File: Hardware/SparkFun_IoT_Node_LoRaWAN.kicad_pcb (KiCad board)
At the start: 4 copper layers, 50.8 x 76.2 mm, 71 parts, among them J1 USB_C_Receptacle, J2 JST_2mm_LiPo, J3 Qwiic_RA, SW1 SMD_4.6x2.8mm_h2.5mm, SW2 SMD_4.6x2.8mm_h2.5mm, U4 W25Q128JVPIM, U5 RT9080-3.3, U6 MCP73831, U7 MAX17048, U8 LM66200, U9 RT9080-3.3

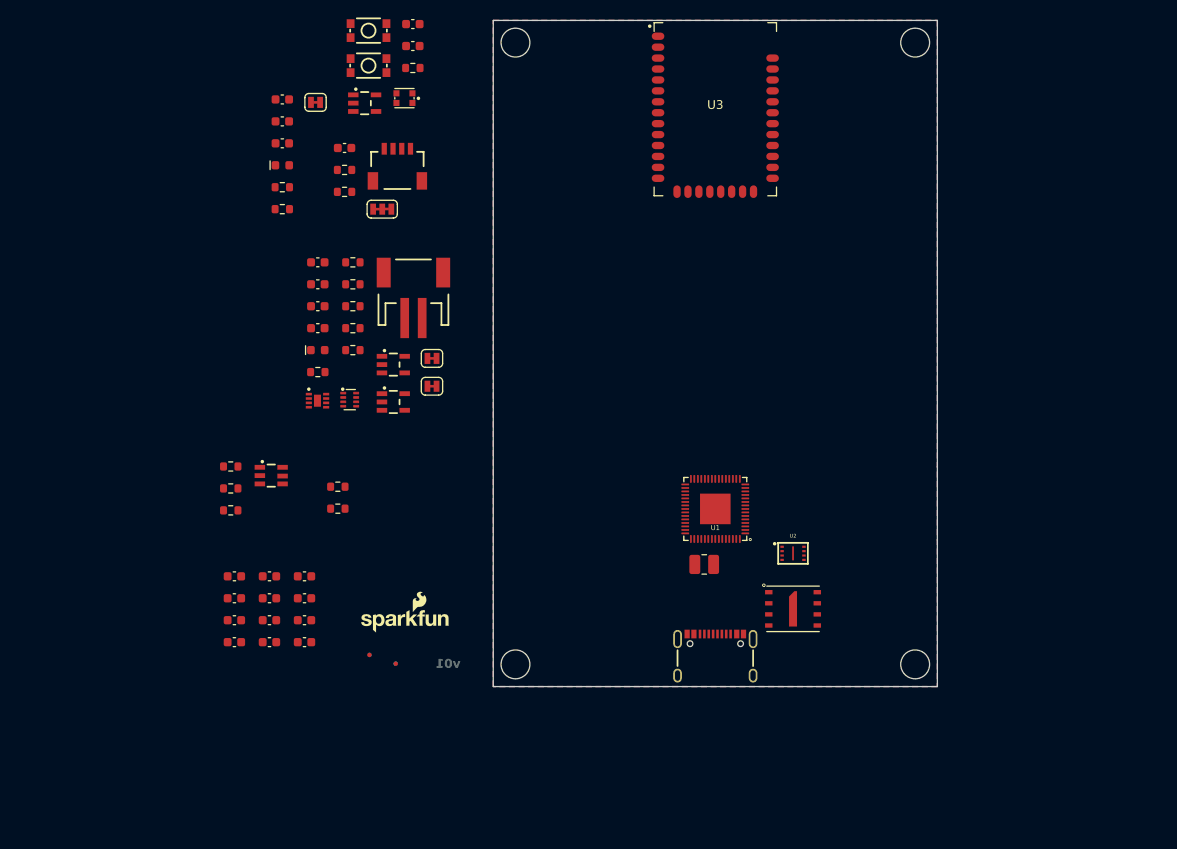
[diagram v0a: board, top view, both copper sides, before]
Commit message: v01 schematic updates
Add remaining schematic components
Split schematic into multiple sheets
Still need to define pinouts for RP2350, XBLR, and headers
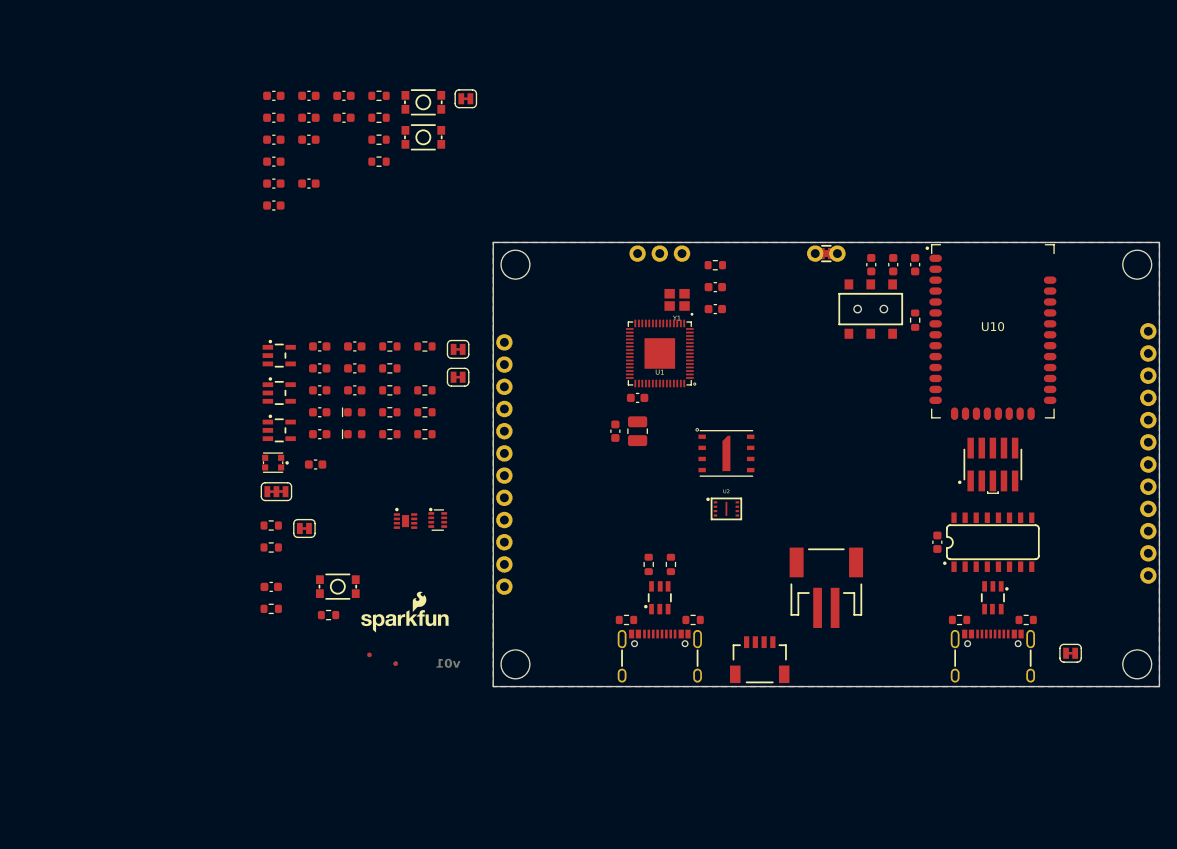
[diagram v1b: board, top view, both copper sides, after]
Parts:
- added C23: 10uF, SparkFun-Capacitor:C_0603_1608Metric, F.Cu at (158.8, 76.2)
- added C24: 1.0uF, SparkFun-Capacitor:C_0603_1608Metric, F.Cu at (161.3, 76.2)
- added C25: 10pF, SparkFun-Capacitor:C_0603_1608Metric, F.Cu at (163.8, 76.2)
- added C26: 10uF, SparkFun-Capacitor:C_0603_1608Metric, F.Cu at (95.2, 99.1)
- added C27: 0.1uF, SparkFun-Capacitor:C_0603_1608Metric, F.Cu at (166.4, 108.0)
- added C28: 2.2uF, SparkFun-Capacitor:C_0603_1608Metric, F.Cu at (90.2, 113.1)
- added C29: 15pF, SparkFun-Capacitor:C_0603_1608Metric, F.Cu at (141.0, 81.3)
- added C30: 15pF, SparkFun-Capacitor:C_0603_1608Metric, F.Cu at (141.0, 78.8)
- added D5: DT1042-04SO, SparkFun-Semiconductor-Standard:SOT23-6, F.Cu at (172.7, 114.3)
- added J4: USB_C_Receptacle, SparkFun-Connector:USB-C_16, F.Cu at (172.7, 118.1)
- added J5: USB_C_Receptacle, SparkFun-Connector:USB-C_16, F.Cu at (134.6, 118.1)
- added J6: SWD, SparkFun-Connector:2x5_1.27mm_SMD_Unshrouded, F.Cu at (172.7, 99.1)
- added J7: Conn_01x12, SparkFun-Connector:1x12, F.Cu at (116.8, 85.1)
- added J8: Conn_01x12, SparkFun-Connector:1x12, F.Cu at (190.5, 83.8)
- added JP5: ~, SparkFun-Jumper:Jumper_2_NC_Trace, F.Cu at (181.6, 120.7)
- added JP6: Measure, SparkFun-Jumper:Jumper_2_PTH_SMD_Combo-NC, F.Cu at (153.7, 74.9)
- added JP7: ~, SparkFun-Jumper:Jumper_2_NC_Trace, F.Cu at (94.0, 106.4)
- added R17: 5.1k, SparkFun-Resistor:R_0603_1608Metric, F.Cu at (176.5, 116.8)
- added R18: 5.1k, SparkFun-Resistor:R_0603_1608Metric, F.Cu at (168.9, 116.8)
- added R19: 100k, SparkFun-Resistor:R_0603_1608Metric, F.Cu at (107.8, 93.1)
- added R20: 2.2k, SparkFun-Resistor:R_0603_1608Metric, F.Cu at (107.8, 95.6)
- added R21: 10k, SparkFun-Resistor:R_0603_1608Metric, F.Cu at (96.7, 116.3)
- added R22: 10k, SparkFun-Resistor:R_0603_1608Metric, F.Cu at (163.8, 82.5)
- added R23: 10, SparkFun-Resistor:R_0603_1608Metric, F.Cu at (90.2, 115.6)
- added R24: 1k, SparkFun-Resistor:R_0603_1608Metric, F.Cu at (90.2, 108.5)
- added R25: 1k, SparkFun-Resistor:R_0603_1608Metric, F.Cu at (141.0, 76.3)
- added SW3: DPDT_Slide_SMD_7.2x3.5mm, SparkFun-Switch:Slide_DPDT_SMD_7.2x3.5mm, F.Cu at (158.8, 81.3)
- added SW4: SMD_4.6x2.8mm_h2.5mm, SparkFun-Switch:Push_SMD_4.6x2.8mm, F.Cu at (97.8, 113.0)
- added U10: ~, SparkFun_IoT_Node_LoRaWAN:XBee_LR, F.Cu at (172.7, 83.8)
- added Y1: ~, SparkFun-Clocks:CRYSTAL-SMD-2X2.5MM, F.Cu at (136.6, 80.2)
- C2, C6: value 2.2uF -> 0.1uF
- C20: value 0.1uF -> 10uF
- C22: value 10uF -> 0.1uF
- C5, C8: value 0.1uF -> 2.2uF
- D1: value Yellow -> WS2812B; footprint SparkFun-LED:LED_0603_1608Metric -> SparkFun-LED:WS2812-2020
- D2: value WS2812B -> Yellow; footprint SparkFun-LED:WS2812-2020 -> SparkFun-LED:LED_0603_1608Metric
- J1: value USB_C_Receptacle -> Conn_01x03; footprint SparkFun-Connector:USB-C_16 -> SparkFun-Connector:1x03
- JP3: footprint SparkFun-Jumper:Jumper_3_NC-2_Trace -> SparkFun-Jumper:Jumper_2_NC_Trace
- JP4: footprint SparkFun-Jumper:Jumper_2_NC_Trace -> SparkFun-Jumper:Jumper_3_NC-2_Trace
- R10, R9: value 2.2k -> 4.7k
- R11: value 100k -> 2.2k
- R13: value 4.7k -> 2.2k
- R5, R6: value 100k -> 10k
- R8: value 4.7k -> 100k
- U3: value ~ -> CH340C; footprint SparkFun_IoT_Node_LoRaWAN:XBee_LR -> SparkFun-Semiconductor-Standard:SO-16
- U5: value RT9080-3.3 -> LM66200; footprint SparkFun-Semiconductor-Standard:SOT23-5 -> SparkFun-Semiconductor-Standard:SOT-583-8
- U6: value MCP73831 -> RT9080-3.3
- U7: value MAX17048 -> MCP73831; footprint SparkFun-Semiconductor-Standard:DFN-8 -> SparkFun-Semiconductor-Standard:SOT23-5
- U8: value LM66200 -> MAX17048; footprint SparkFun-Semiconductor-Standard:SOT-583-8 -> SparkFun-Semiconductor-Standard:DFN-8
- moved J3 70.0 mm to (146.1, 119.4)
- moved C21 60.2 mm to (98.5, 56.9)
- moved C22 60.2 mm to (98.5, 59.4)
- moved U3 58.8 mm to (172.7, 108.0), turned to 90 degrees
- moved J2 57.7 mm to (153.7, 111.8)
- moved C17 55.1 mm to (94.5, 61.9)
- moved C15 55.1 mm to (94.5, 56.9)
- moved C16 55.1 mm to (94.5, 59.4)
- moved R11 54.8 mm to (90.2, 106.0)
- moved C13 50.1 mm to (90.5, 66.9)
- moved C11 50.1 mm to (90.5, 61.9)
- moved C12 50.1 mm to (90.5, 64.4)
- moved C14 50.1 mm to (90.5, 69.4)
- moved R4 48.4 mm to (133.3, 110.5), turned to -90 degrees
- moved D4 46.6 mm to (134.6, 114.3), turned to 90 degrees
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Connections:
- C12 pad 1: 3.3V -> 1.1V
- C14 pad 1: 3.3V -> 1.1V
- C16 pad 1: 3.3V -> 1.1V
- C18 pad 1: 3.3V -> 1.1V
- C19 pad 1: 1.8V -> 3.3V
- C2 pad 1: 3.3V -> 3.3V_P
- C20 pad 1: 1.8V -> 3.3V
- C21 pad 1: 1.8V -> 3.3V
- C22 pad 1: 1.8V -> 3.3V
- C3 pad 1: VBUS -> 3.3V
- C4 pad 1: VBATT -> VBUS
- C6 pad 1: VIN -> VBATT
- C7 pad 1: 3.3V_P -> VIN
- D1 pad 1: Net-(D1-K) -> LED_OUT
- D1 pad 2: Net-(D1-A) -> GND
- D2 pad 1: LED_OUT -> Net-(D2-K)
- D2 pad 2: GND -> Net-(D2-A)
- JP1 pad 1: Net-(J1-SHIELD) -> Net-(J5-SHIELD)
- JP2 pad 2: Net-(D1-A) -> Net-(D2-A)
- JP3 pad 2: 3.3V_P -> 3.3V
- JP4 pad 2: 3.3V -> 3.3V_P
- L1 pad 1: 1.8V -> 1.1V
- R1 pad 1: Net-(J1-CC2) -> Net-(J5-CC2)
- R10 pad 2: SCL -> Net-(D3-A)
- R11 pad 1: PERIPHERAL_POWER -> Net-(U7-PROG)
- R11 pad 2: 3.3V -> GND
- R12 pad 2: ~{BOOT} -> PSRAM_~{CS}
- R13 pad 1: Net-(JP4-A) -> Net-(JP4-B)
- R13 pad 2: Net-(D3-A) -> SDA
- R14 pad 2: QSPI_~{CS} -> ~{RESET}
- R16 pad 2: PSRAM_~{CS} -> QSPI_~{CS}
- R2 pad 1: Net-(J1-CC1) -> Net-(J5-CC1)
- R5 pad 1: Net-(U5-EN) -> 3.3V
- R5 pad 2: VIN -> REGION
- R6 pad 1: 3.3V -> REGION
- R6 pad 2: BAT_POWER -> GND
- R7 pad 1: Net-(U6-PROG) -> 3.3V
- R7 pad 2: GND -> BAT_POWER
- R8 pad 1: VBUS -> ~{ON}
- R8 pad 2: Net-(JP2-A) -> GND
- R9 pad 1: Net-(JP3-B) -> VBUS
- R9 pad 2: SDA -> Net-(JP2-A)
- SW1 pad 2: ~{RESET} -> ~{BOOT}
- SW2 pad 2: ~{BOOT} -> ~{RESET}
- U1 pad 21: unconnected-(U1-XIN-Pad21) -> Net-(U1-XIN)
- U1 pad 22: unconnected-(U1-XOUT-Pad22) -> Net-(U1-XOUT)
- U1 pad 23: 1.8V -> 1.1V
- U1 pad 24: unconnected-(U1-SWCLK-Pad24) -> RP2350_SWCLK
- U1 pad 25: unconnected-(U1-SWDIO-Pad25) -> RP2350_SWDIO
- U1 pad 39: 1.8V -> 1.1V
- U1 pad 50: 1.8V -> 1.1V
- U1 pad 6: 1.8V -> 1.1V
- U3 pad 10: GND -> unconnected-(U3-~{DSR}-Pad10)
- U3 pad 12: GND -> unconnected-(U3-~{DCD}-Pad12)
- U3 pad 16: unconnected-(U3-SPI_MISO/DIO15-Pad16) -> 3.3V
- U3 pad 2: 3.3V -> XBLR_USB_TX
- U3 pad 3: XBLR_TX -> XBLR_USB_RX
- U3 pad 4: XBLR_RX -> 3.3V
- U3 pad 5: unconnected-(U3-DIO12-Pad5) -> XBLR_USB_DP
- U3 pad 6: unconnected-(U3-~{RESET}-Pad6) -> XBLR_USB_DN
- U5 pad 1: VIN -> GND
- U5 pad 2: GND -> VIN
- U5 pad 3: Net-(U5-EN) -> VBATT
- U5 pad 4: unconnected-(U5-NC-Pad4) -> ~{ON}
- U5 pad 5: 3.3V -> GND
- U6 pad 1: Net-(D1-K) -> VIN
- U6 pad 3: VBATT -> VIN
- U6 pad 4: VBUS -> unconnected-(U6-NC-Pad4)
- U6 pad 5: Net-(U6-PROG) -> 3.3V
- U7 pad 1: GND -> Net-(D2-K)
- U7 pad 2: VBATT -> GND
- U7 pad 3: unconnected-(U7-VDD-Pad3) -> VBATT
- U7 pad 4: GND -> VBUS
- U7 pad 5: FUEL_GAUGE_~{ALRT} -> Net-(U7-PROG)
- U8 pad 2: VIN -> VBATT
- U8 pad 3: VBATT -> unconnected-(U8-VDD-Pad3)
- U8 pad 5: GND -> FUEL_GAUGE_~{ALRT}
- U8 pad 6: VBUS -> GND
- U8 pad 7: VIN -> SCL
- U8 pad 8: BAT_POWER -> SDA
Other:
- board size 50.8 x 76.2 mm -> 76.2 x 50.8 mm

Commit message: Initial board layout
Board outline determined based off selected enclosure
Clusters of components placed and routed
Waiting for feedback before finishing routing
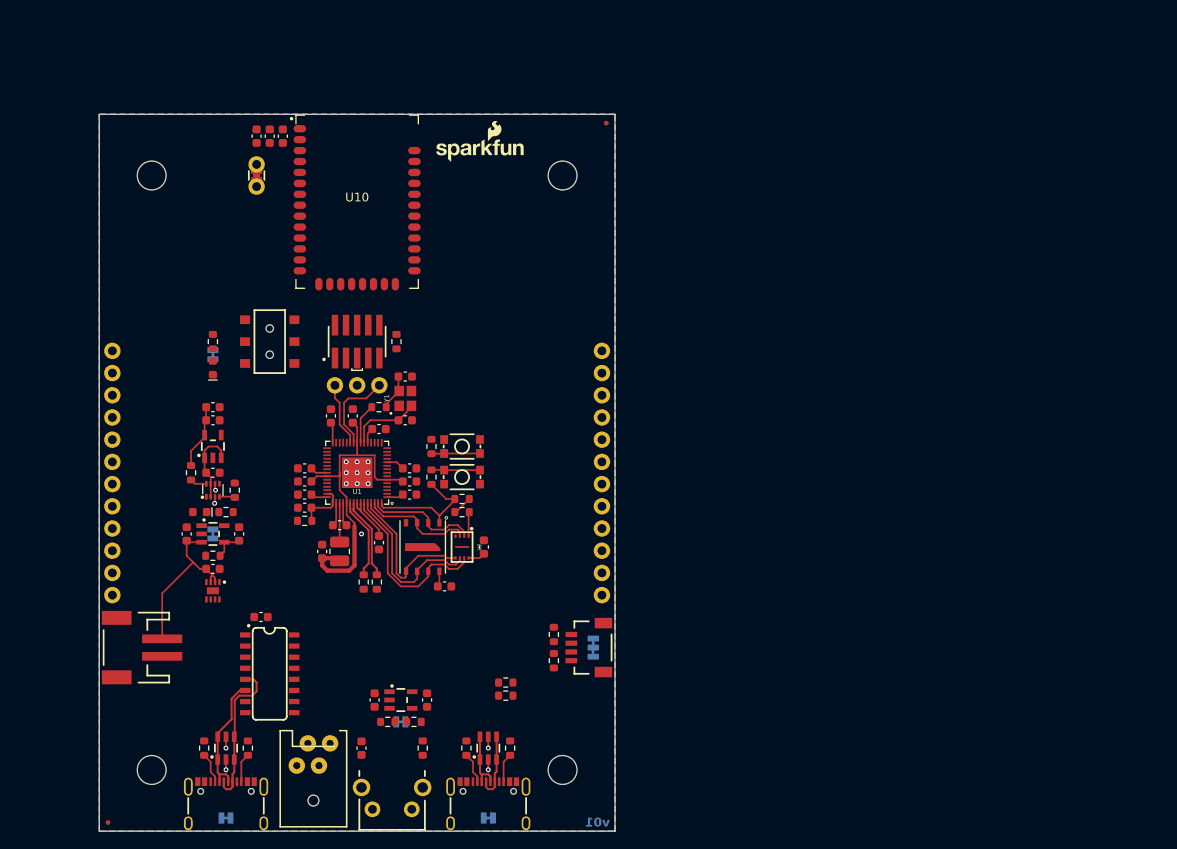
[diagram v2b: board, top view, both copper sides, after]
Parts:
- D1: value WS2812B -> WS2812B_CBI; footprint SparkFun-LED:WS2812-2020 -> SparkFun-LED:WS2812B-CBI
- JP1, JP2, JP3, JP4, JP5, JP7: moved to B.Cu
- ST1, ST2, ST3, ST4: value Stand_off -> Standoff
- SW4: value SMD_4.6x2.8mm_h2.5mm -> PTH_RA_h7.5mm; footprint SparkFun-Switch:Push_SMD_4.6x2.8mm -> SparkFun-Switch:Push_PTH_RA_8-020_h7.5mm
- moved J8 122.3 mm to (72.0, 114.0), turned to 90 degrees
- moved ST4 113.4 mm to (76.5, 134.0)
- moved JP5 98.4 mm to (85.0, 139.5), turned to 180 degrees
- moved R17 90.2 mm to (87.5, 131.5), turned to 90 degrees
- moved D5 89.4 mm to (85.0, 131.5), turned to 90 degrees
- moved J4 89.3 mm to (85.0, 135.0)
- moved R18 87.6 mm to (82.5, 131.5), turned to 90 degrees
- moved ST3 87.5 mm to (123.5, 134.0)
- moved U3 84.1 mm to (90.0, 123.0), turned to 0 degrees
- moved JP1 82.3 mm to (115.0, 139.5), turned to 180 degrees
- moved J2 80.1 mm to (74.0, 120.0), turned to 90 degrees
- moved C27 77.8 mm to (89.0, 116.5), turned to 180 degrees
- moved U10 74.2 mm to (100.0, 69.0)
- moved J6 74.1 mm to (100.0, 85.0)
- moved C25 73.8 mm to (91.5, 61.5)
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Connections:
- net Net-(D4-I/O1) renamed /RP2350/USB_D-
- net Net-(D4-I/O2) renamed /RP2350/USB_D+
- net USB_DN renamed RP2350_USB_D-
- net USB_DP renamed RP2350_USB_D+
- net XBLR_USB_DN renamed XBLR_USB_D-
- net XBLR_USB_DP renamed XBLR_USB_D+
- D1 pad 1: LED_OUT -> LED_IN
- D1 pad 2: GND -> 3.3V_P
- D1 pad 3: LED_IN -> GND
- D1 pad 4: 3.3V_P -> LED_OUT
- U8 pad 3: unconnected-(U8-VDD-Pad3) -> VBATT
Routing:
- net 1.1V: track 0.00 -> 38.2 mm
- net 3.3V: track 0.00 -> 33.9 mm
- net QSPI_D3: track 0.00 -> 21.2 mm
- net VBATT: track 0.00 -> 20.1 mm, vias 0 -> 1
- net QSPI_SCLK: track 0.00 -> 19.7 mm
- net QSPI_D0: track 0.00 -> 17.9 mm
- net XBLR_USB_D+: track 0.00 -> 17.2 mm
- net QSPI_~{CS}: track 0.00 -> 14.3 mm
- net XBLR_USB_D-: track 0.00 -> 13.9 mm
- net QSPI_D1: track 0.00 -> 13.0 mm
- net QSPI_D2: track 0.00 -> 13.0 mm
- net RP2350_SWCLK: track 0.00 -> 9.89 mm
- net RP2350_USB_D-: track 0.00 -> 9.35 mm
- net RP2350_USB_D+: track 0.00 -> 9.35 mm
- net VIN: track 0.00 -> 8.70 mm
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- added copper zone on In2.Cu, net 3.3V
- added copper zone on B.Cu, net GND
- added copper zone on F.Cu, net GND
- added copper zone on In1.Cu, net GND
- removed copper zone on B.Cu, net (none)
- removed copper zone on F.Cu, net (none)
- removed copper zone on In1.Cu, net (none)
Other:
- board size 76.2 x 50.8 mm -> 59 x 82 mm

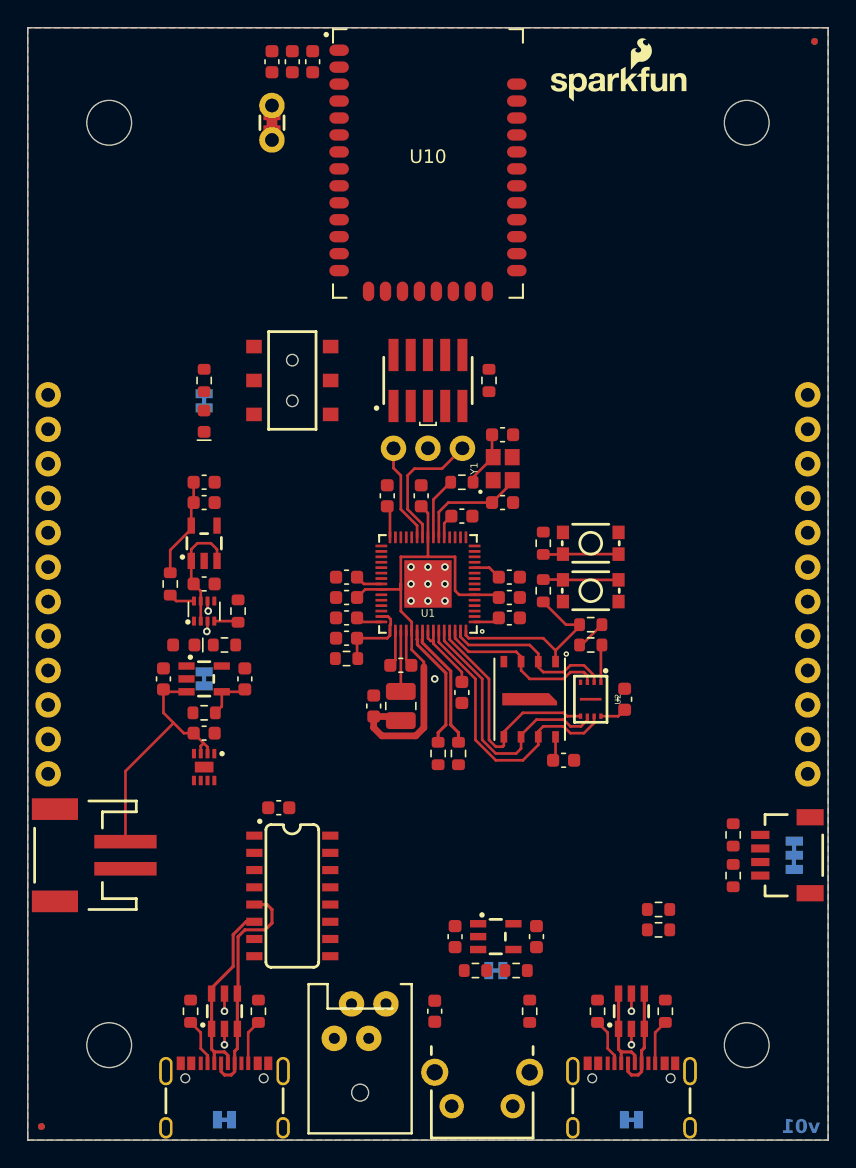
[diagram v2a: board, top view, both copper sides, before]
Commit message: Review updates
Remove region selection resistors
Add uSD card connector
Move XBLR USB connector within enclosure
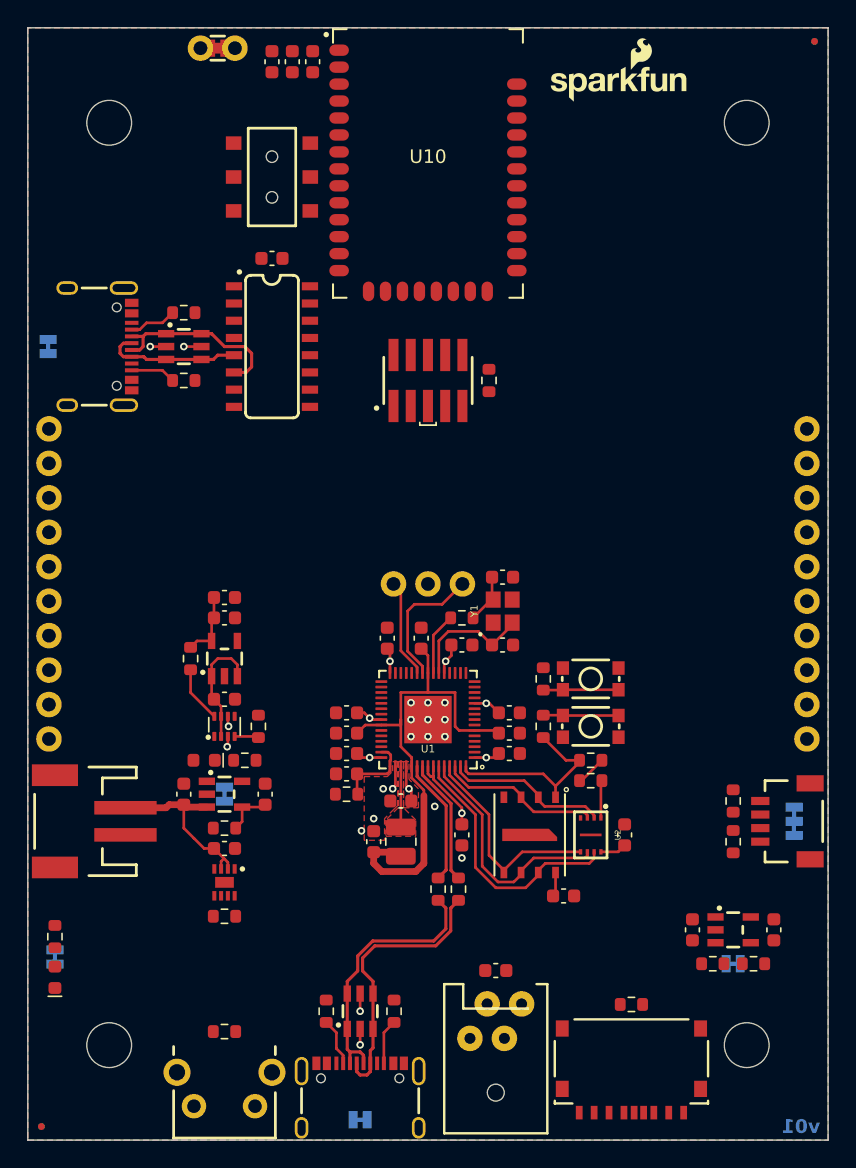
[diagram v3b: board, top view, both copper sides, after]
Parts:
- added J9: microSD_Friction, SparkFun-Connector:microSD_Friction_Fit_Atom, F.Cu at (115.0, 135.0)
- J7, J8: footprint SparkFun-Connector:1x12 -> SparkFun-Connector:1x10
- moved JP5 58.5 mm to (72.0, 82.5), turned to 90 degrees
- moved J7 56.0 mm to (72.1, 111.4)
- moved J8 56.0 mm to (127.9, 111.4)
- moved J4 52.9 mm to (78.5, 82.5), turned to -90 degrees
- moved R18 51.5 mm to (82.0, 80.0), turned to 0 degrees
- moved D5 49.1 mm to (82.0, 82.5), turned to 0 degrees
- moved R17 46.8 mm to (82.0, 85.0), turned to 0 degrees
- moved D3 42.4 mm to (72.5, 129.0)
- moved JP3 42.4 mm to (72.5, 127.5)
- moved R10 42.4 mm to (72.5, 126.0)
- moved U3 40.5 mm to (88.5, 82.5)
- moved C27 40.5 mm to (88.5, 76.0)
- moved R6 32.0 mm to (85.0, 124.5)
- moved R21 22.5 mm to (85.0, 133.0), turned to 0 degrees
- moved D4 20.0 mm to (95.0, 131.5)
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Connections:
- R5 pad 1: 3.3V -> SD_DET
- R5 pad 2: REGION -> GND
- R6 pad 1: REGION -> 3.3V
- R6 pad 2: GND -> FUEL_GAUGE_~{ALRT}
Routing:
- net /RP2350/USB_D+: track 7.65 -> 20.4 mm
- net /RP2350/USB_D-: track 6.92 -> 19.7 mm
- net XBLR_USB_D+: track 17.2 -> 10.2 mm
- net VBATT: track 20.1 -> 14.3 mm
- net BAT_POWER: track 1.93 -> 4.16 mm
- net QSPI_D0: track 17.9 -> 15.9 mm
- net 3.3V: track 33.9 -> 32.0 mm, vias 0 -> 8
- net QSPI_SCLK: track 19.7 -> 18.0 mm
- net QSPI_D3: track 21.2 -> 19.5 mm
- net QSPI_D2: track 13.0 -> 12.0 mm
- net GND: track 5.07 -> 4.10 mm, vias 12 -> 17
- net QSPI_D1: track 13.0 -> 12.1 mm
- net Net-(U1-XIN): track 8.34 -> 9.25 mm
- net 1.1V: track 38.2 -> 37.7 mm
- added copper zone on F.Cu, net 3.3V
- added copper zone on F.Cu, net Net-(U1-VREG_LX)
